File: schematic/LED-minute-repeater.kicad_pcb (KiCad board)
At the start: 2 copper layers, 29.5 x 38.1 mm, 24 parts, among them J1 ICSP, J2 WS2812B_OUT, J3 I2C, SW2 Hour, SW3 Minute, U1 ATTiny85, U2 DS3231, U3 MCP1700T

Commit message: fix reg and RTC chip pin assign swap
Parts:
- moved SW3 2.24 mm to (144.0, 112.1)
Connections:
- R1 pad 2: RTC_SCL -> RTC_SDA
- R7 pad 2: RTC_SDA -> RTC_SCL
- U2 pad 15: RTC_SCL -> RTC_SDA
- U2 pad 16: RTC_SDA -> RTC_SCL
- U3 pad 2: +3V3 -> +5V
- U3 pad 3: +5V -> +3V3
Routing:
- net +3V3: track 22.5 -> 9.69 mm
- net RTC_SDA: track 60.3 -> 51.1 mm
- net RTC_SCL: track 54.0 -> 57.0 mm
- net +5V: track 11.4 -> 14.1 mm
- net (no net): track 0.00 -> 1.50 mm
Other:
- board text added: "LED Minites Repeater Clock Rev 0.2"
- board text removed: "LED Minites Repeater Clock Rev 0.1"

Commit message: PCB layout for rev 0.2 circuit
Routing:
- net RTC_SCL: track 57.0 -> 51.8 mm
- net (no net): track 1.50 -> 0.00 mm
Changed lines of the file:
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@@
     (links 55)
     (no_connects 1)
-    (area 125.083499 76.061499 154.697501 114.311501)
+    (area 114.579448 73.828 178.513201 122.460182)
     (thickness 1.6)
     (drawings 29)
-    (tracks 121)
+    (tracks 116)
     (zones 0)
     (modules 24)
@@
   (gr_arc (start 152.0825 78.6765) (end 152.0825 76.1365) (angle 90) (layer Edge.Cuts) (width 0.15))
   (gr_arc (start 127.6985 78.6765) (end 125.1585 78.6765) (angle 90) (layer Edge.Cuts) (width 0.15))
-  (segment (start 151.892 100.457) (end 151.892 98.9584) (width 0.2032) (layer B.Cu) (net 0))
   (segment (start 142.8514 108.8644) (end 144.0688 108.8644) (width 0.3) (layer B.Cu) (net 1))
   (segment (start 146.7866 105.3846) (end 145.2372 103.8352) (width 0.3) (layer B.Cu) (net 1))
@@
   (segment (start 140.2842 89.4842) (end 140.2842 86.2838) (width 0.2032) (layer F.Cu) (net 5))
   (segment (start 140.2842 86.2838) (end 138.9888 84.9884) (width 0.2032) (layer F.Cu) (net 5))
-  (segment (start 151.8666 100.4062) (end 151.8666 99.5172) (width 0.2032) (layer F.Cu) (net 6))
   (segment (start 148.336 99.822) (end 145.4404 99.822) (width 0.2032) (layer F.Cu) (net 6))
   (segment (start 145.4404 99.822) (end 137.668 92.0496) (width 0.2032) (layer F.Cu) (net 6))
@@
   (segment (start 148.336 110.617) (end 147.5486 111.4044) (width 0.2032) (layer B.Cu) (net 6))
   (segment (start 148.336 99.822) (end 148.336 99.9744) (width 0.2032) (layer F.Cu) (net 6))
-  (segment (start 148.336 99.9744) (end 149.5552 101.1936) (width 0.2032) (layer F.Cu) (net 6))
-  (segment (start 149.5552 101.1936) (end 151.0792 101.1936) (width 0.2032) (layer F.Cu) (net 6))
-  (segment (start 151.0792 101.1936) (end 151.8666 100.4062) (width 0.2032) (layer F.Cu) (net 6))
   (segment (start 130.6957 90.0557) (end 128.0795 90.0557) (width 0.2032) (layer F.Cu) (net 6))
   (segment (start 127.2794 87.9856) (end 129.0828 86.1822) (width 0.2032) (layer F.Cu) (net 6))

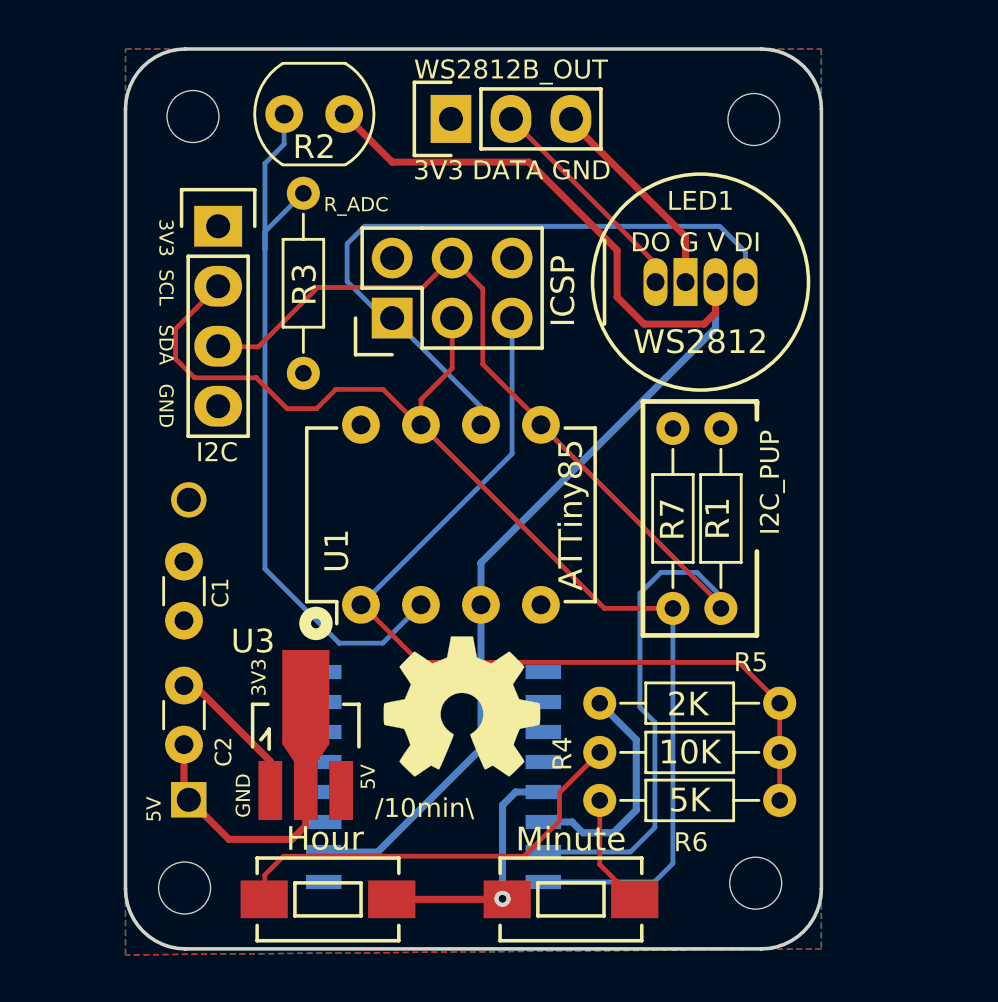
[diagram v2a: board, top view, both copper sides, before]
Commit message: Smaller size SMD version of PCB
OSH Order #MdFUZar9
Erratta:
    - I2C GND is not connected
    - Reg (MCP1700) GND is not connected
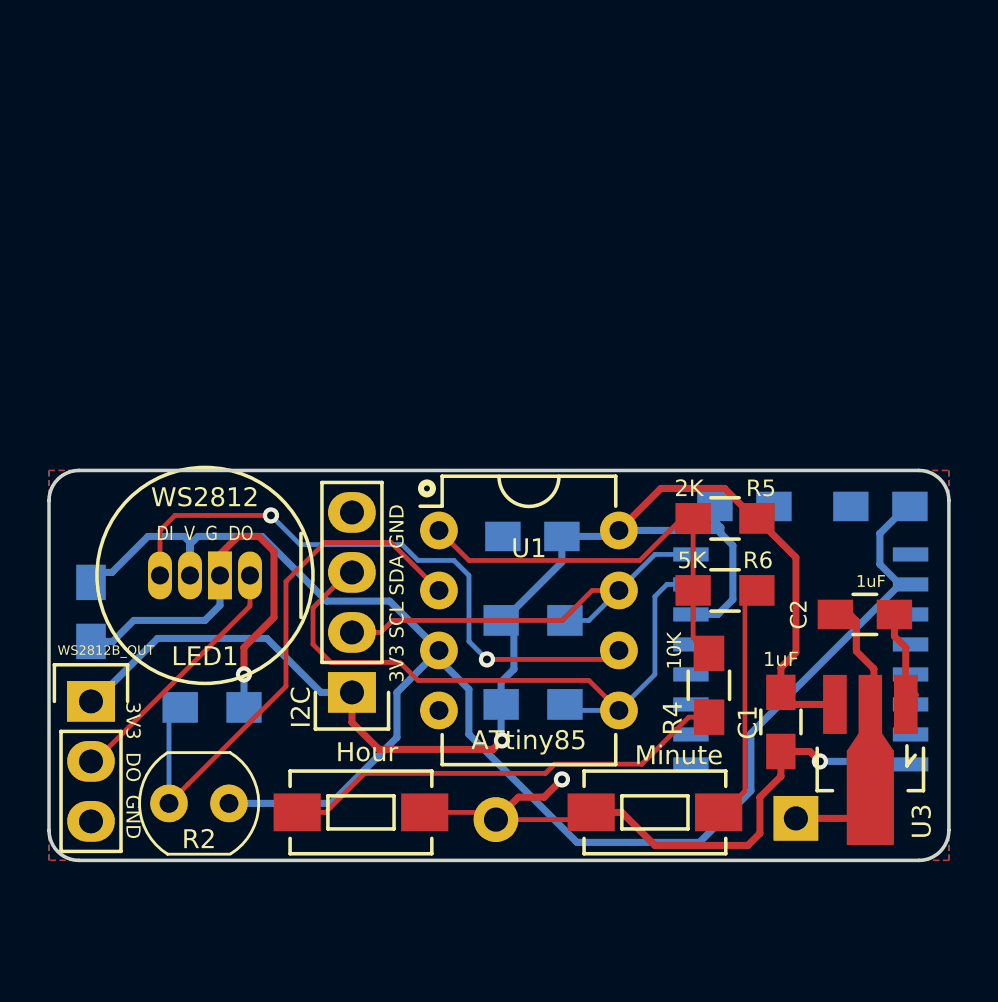
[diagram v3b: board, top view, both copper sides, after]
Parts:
- removed J1: ICSP, Pin_Headers:Pin_Header_Straight_2x03
- removed REF** (x4): MountingHole_2.2mm_M2_ISO7380, Mounting_Holes:MountingHole_2.2mm_M2_ISO7380
- removed REF***: OSHW-Symbol_6.7x6mm_SilkScreen, Symbols:OSHW-Symbol_6.7x6mm_SilkScreen
- added C3: 0.1uF (LED), Capacitors_SMD:C_0805_HandSoldering, B.Cu at (123.7, 100.0)
- added C4: 0.1uF (RTC Vbat), Capacitors_SMD:C_0805_HandSoldering, B.Cu at (151.4, 95.5)
- added C5: 0.1uF (RTC Vcc), Capacitors_SMD:C_0805_HandSoldering, B.Cu at (157.1, 95.5)
- added C6: 0.1uF (AT85), Capacitors_SMD:C_0805_HandSoldering, B.Cu at (142.4, 96.8)
- C1, C2: footprint Capacitors_THT:C_Disc_D3.0mm_W1.6mm_P2.50mm -> Capacitors_SMD:C_0805_HandSoldering
- R1: value I2C_PUP -> SDA_PUP; footprint Resistors_THT:R_Axial_DIN0204_L3.6mm_D1.6mm_P7.62mm_Horizontal -> Resistors_SMD:R_0805_HandSoldering; moved to B.Cu
- R3: footprint Resistors_THT:R_Axial_DIN0204_L3.6mm_D1.6mm_P7.62mm_Horizontal -> Resistors_SMD:R_0805_HandSoldering; moved to B.Cu
- R4, R5, R6: footprint Resistors_THT:R_Axial_DIN0204_L3.6mm_D1.6mm_P7.62mm_Horizontal -> Resistors_SMD:R_0805_HandSoldering
- R7: value I2C_PUP -> SCL_PUP; footprint Resistors_THT:R_Axial_DIN0204_L3.6mm_D1.6mm_P7.62mm_Horizontal -> Resistors_SMD:R_0805_HandSoldering; moved to B.Cu
- U1: value ATTiny85 -> ATtiny85
- moved R2 29.6 mm to (129.5, 108.1)
- moved C2 29.4 mm to (156.5, 100.1), turned to 0 degrees
- moved J2 29.0 mm to (123.7, 103.8), turned to 0 degrees
- moved C1 26.2 mm to (152.9, 104.6)
- moved BT1 25.7 mm to (153.5, 108.7), turned to 90 degrees
- moved LED1 24.4 mm to (128.5, 98.4), turned to 0 degrees
- moved U3 23.9 mm to (156.7, 106.2), turned to 180 degrees
- moved R3 22.1 mm to (128.8, 104.0), turned to 0 degrees
- moved J3 20.5 mm to (134.7, 103.4), turned to 180 degrees
- moved U2 16.3 mm to (153.7, 102.0), turned to 180 degrees
- moved R1 14.1 mm to (142.4, 103.9), turned to 0 degrees
- moved R7 10.1 mm to (142.4, 100.3), turned to 0 degrees
- moved R5 9.45 mm to (150.5, 96.0), turned to 180 degrees
- moved R6 9.19 mm to (150.5, 99.1), turned to 0 degrees
- moved SW3 5.12 mm to (147.6, 108.5)
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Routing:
- net +3V3: track 9.69 -> 64.0 mm, vias 0 -> 1
- net RTC_SCL: track 51.8 -> 18.5 mm
- net GND: track 25.9 -> 51.1 mm, vias 1 -> 3
- net RTC_SDA: track 51.1 -> 27.5 mm
- net BUTTON/RST: track 38.4 -> 18.1 mm
- net PWR_CTRL: track 54.4 -> 68.1 mm
- net PCELL: track 31.2 -> 23.7 mm
- net +5V: track 14.1 -> 8.42 mm
- net Net-(R6-Pad2): track 4.80 -> 10.3 mm
- net LED_SIG: track 29.1 -> 26.4 mm, vias 0 -> 2
- net LED_SIG_OUT: track 9.44 -> 10.8 mm
- net Net-(R4-Pad2): track 18.0 -> 19.2 mm
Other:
- board size 29.5 x 38.1 mm -> 38.1 x 16.5 mm
- board text added: "3V3 DO GND"
- board text added: "DI V G DO"
- board text added: "LED Minute Repeater Clock rev 0.5 2017-04-30 @ryo1kato"
- board text removed: "/10min\"
- board text removed: "2017-04-17 @ryo1kato"
- board text removed: "3V3"
- board text removed: "3V3 DATA GND"
- board text removed: "5V"
- board text removed: "DO G V DI"
- board text removed: "GND"
- board text removed: "LED Minites Repeater Clock Rev 0.2"

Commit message: rev 0.5.1 - errata fix for rev0.5
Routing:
- net GND: track 51.1 -> 59.7 mm, vias 3 -> 4
- net +5V: track 8.42 -> 12.4 mm
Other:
- board text added: "LED Minute Repeater Clock rev 0.5.1 2017-04-30 @ryo1kato"
- board text removed: "LED Minute Repeater Clock rev 0.5 2017-04-30 @ryo1kato"
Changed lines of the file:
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@@
 (kicad_pcb (version 4) (host pcbnew 4.0.6)
   (general
-    (links 0)
-    (no_connects 3)
+    (links 57)
+    (no_connects 0)
     (area 121.844999 93.904999 160.095001 110.565001)
     (thickness 1.6)
     (drawings 15)
-    (tracks 200)
+    (tracks 210)
     (zones 0)
     (modules 22)
@@
     (effects (font (size 0.6 0.5) (thickness 0.08)))
   )
-  (gr_text "LED Minute Repeater Clock rev 0.5\n2017-04-30\n@ryo1kato " (at 134.874 107.696) (layer B.SilkS)
+  (gr_text "LED Minute Repeater Clock rev 0.5.1\n2017-04-30\n@ryo1kato " (at 134.874 107.696) (layer B.SilkS)
     (effects (font (size 0.8 0.6) (thickness 0.07)) (justify mirror))
   )
@@
   (gr_arc (start 123.19 95.25) (end 121.92 95.25) (angle 90) (layer Edge.Cuts) (width 0.15))
   (gr_arc (start 158.75 95.25) (end 158.75 93.98) (angle 90) (layer Edge.Cuts) (width 0.15))
+  (segment (start 156.69514 105.48874) (end 156.69514 107.83824) (width 0.3) (layer F.Cu) (net 1))
+  (segment (start 156.69514 103.886) (end 156.69514 105.48874) (width 0.3) (layer F.Cu) (net 1))
   (segment (start 156.69514 103.886) (end 156.845 103.73614) (width 0.3) (layer F.Cu) (net 1))
   (segment (start 156.845 103.73614) (end 156.845 102.378) (width 0.3) (layer F.Cu) (net 1))
@@
   (segment (start 153.543 108.712) (end 155.82138 108.712) (width 0.3) (layer F.Cu) (net 1))
   (segment (start 155.82138 108.712) (end 156.69514 107.83824) (width 0.3) (layer F.Cu) (net 1))
+  (segment (start 158.623 107.823) (end 158.623 108.077) (width 0.3) (layer B.Cu) (net 2))
+  (segment (start 158.623 108.077) (end 158.75 108.204) (width 0.3) (layer B.Cu) (net 2))
+  (segment (start 158.19628 104.98328) (end 158.623 105.41) (width 0.3) (layer F.Cu) (net 2))
+  (segment (start 158.623 105.41) (end 158.623 107.823) (width 0.3) (layer F.Cu) (net 2))
+  (via (at 158.623 107.823) (size 0.6858) (drill 0.3302) (layers F.Cu B.Cu) (net 2))
+  (segment (start 158.19628 103.886) (end 158.19628 104.98328) (width 0.3) (layer F.Cu) (net 2))
+  (segment (start 131.445 97.409) (end 133.096 95.758) (width 0.3) (layer F.Cu) (net 2))
+  (segment (start 133.096 95.758) (end 134.747 95.758) (width 0.3) (layer F.Cu) (net 2))
   (segment (start 123.698 101.219) (end 124.623 101.219) (width 0.3) (layer B.Cu) (net 2))
   (segment (start 124.623 101.219) (end 125.512 100.33) (width 0.3) (layer B.Cu) (net 2))
